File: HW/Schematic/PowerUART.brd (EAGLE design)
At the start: 29.1 x 35.4 mm, 62 parts, among them U2 CP2104

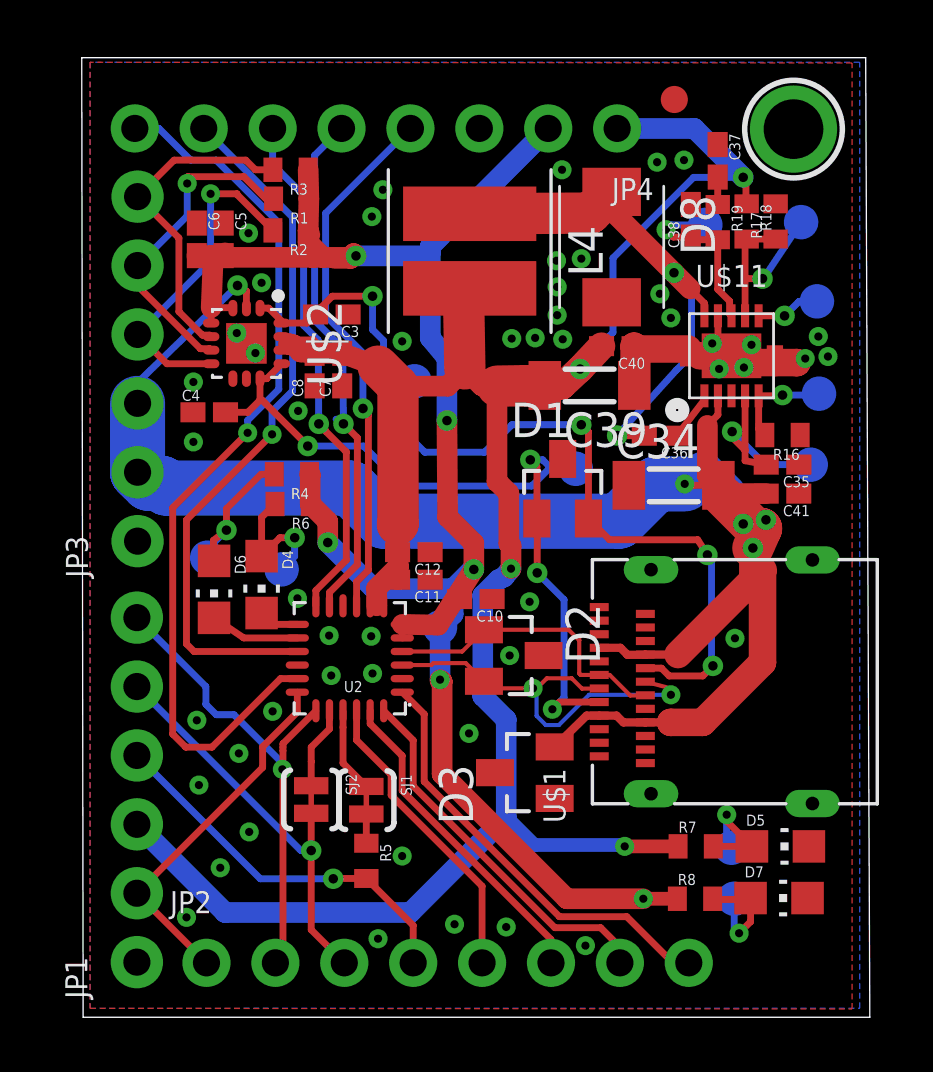
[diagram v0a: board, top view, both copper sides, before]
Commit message: Add labels
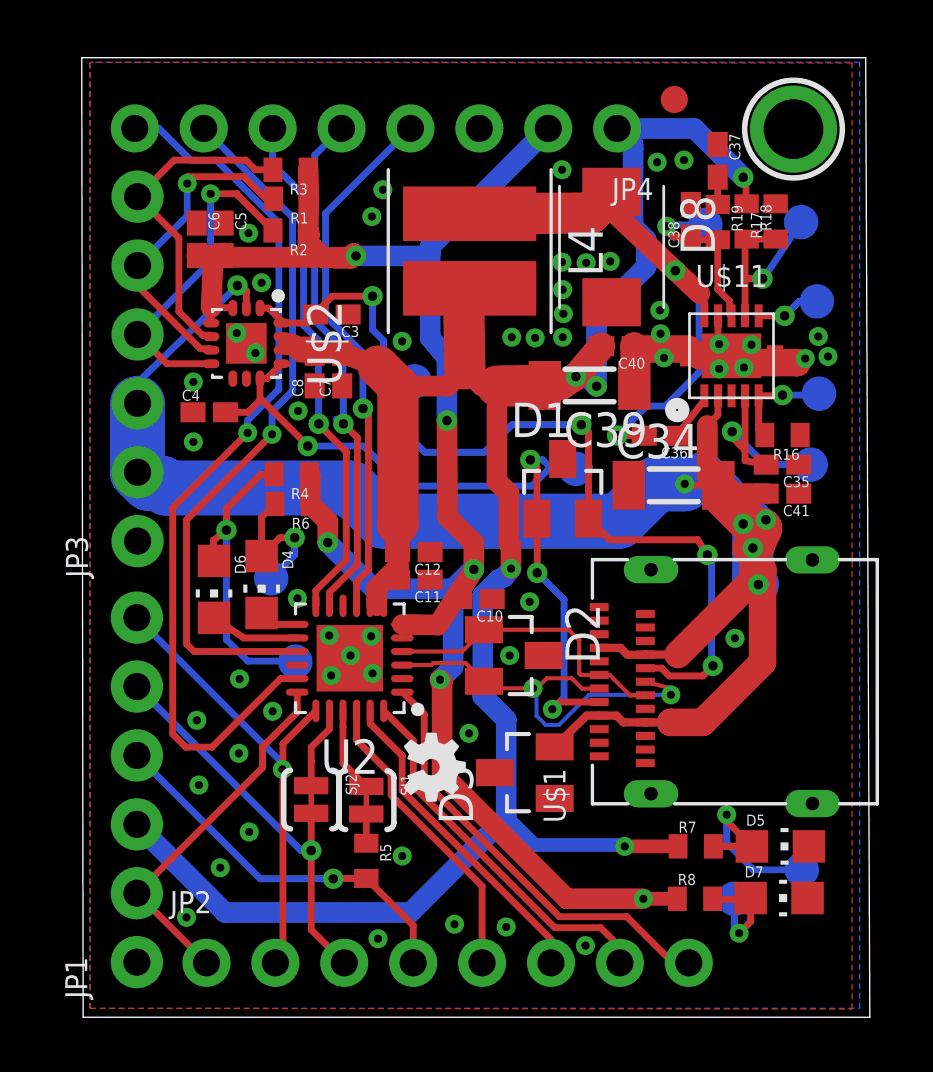
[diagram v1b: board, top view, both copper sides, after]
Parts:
- removed TP10, TP16, TP5, TP6: CP_RESET, testpad:B1,27
- added 5VLEDWP, RXLEDWP, TXLEDWP: CP_RESET, testpad:B1,27
- added LOGO1: OSHW-LOGOMINI, IO_expander:OSHW-LOGO-MINI
- U2: value CP2104 -> CP2104QFN_PAD; device CP2104:QFN50P400X400X100-24 -> CP2104:QFN50P400X400X80-25T245
- renumbered TP1 to SS/TR, TP11 to PGOOD, TP12 to 3V45LEDWP, TP3 to CLK, TP4 to VSNS, TP7 to CC1, TP8 to CC2, TP9 to COMP
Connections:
- net 5VLEDWP: now also 5VLEDWP.TP; no longer TP10.TP
- net CP_VDD_3V45: no longer TP16.TP
- net GND: now also U2.25
- net RXLEDWP: now also RXLEDWP.TP; no longer TP6.TP
- net TXLEDWP: now also TXLEDWP.TP; no longer TP5.TP
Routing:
- net TXLEDWP: track 5.75 -> 11.4 mm
- net 5V: track 90.5 -> 93.6 mm, vias 4 -> 5
- net 5VLEDWP: track 4.27 -> 7.20 mm
- net VBUS: track 68.0 -> 70.5 mm, vias 5 -> 6
- net L1: track 19.9 -> 20.7 mm
- net GND: track 8.31 -> 8.25 mm, vias 50 -> 54
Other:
- board text added: "/INT"
- board text added: "/SUS"
- board text added: "20V 5A max"
- board text added: "3v45"
- board text added: "5V"
- board text added: "CTS"
- board text added: "DCD"
- board text added: "DSR"
- board text added: "DTR"
- board text added: "Engineerd by @bindebende REV A 2018.11.24. github.com/ bindebende/PowerUART"
- board text added: "GND"
- board text added: "GPIO2"
- board text added: "GPIO3"
- board text added: "RESET"
- board text added: "RI"
- board text added: "RTS"
- board text added: "RXD"
- board text added: "SCL"
- board text added: "SDA"
- board text added: "SUS"
- board text added: "TXD"
- board text added: "VBUS"

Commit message: add testpoints.csv
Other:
- board size 29.1 x 35.4 mm -> 29 x 35.5 mm
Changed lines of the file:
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@@
 <setting verticaltext="up"/>
 </settings>
-<grid distance="1" unitdist="mil" unit="mil" style="lines" multiple="1" display="yes" altdistance="0.000123031496" altunitdist="mil" altunit="mil"/>
+<grid distance="1" unitdist="mil" unit="mm" style="lines" multiple="1" display="yes" altdistance="0.000123031496" altunitdist="mil" altunit="mil"/>
 <layers>
 <layer number="1" name="Top" color="4" fill="1" visible="yes" active="yes"/>
@@
 <fusionsync huburn="a.cGVyc29uYWw6dWUyOTdhZGZi" projecturn="a.cGVyc29uYWw6dWUyOTdhZGZiIzIwMTYwMTA4MjIzOTY3MjY" f3durn="urn:adsk.wipprod:dm.lineage:jQXCEEFlSgyEhEQMhi0FtQ" pcbguid="53d00ac5-8cbc-41ab-bffd-7753b437712b" lastpulledtime="" lastsyncedchangeguid="e1987d31-fde6-4ada-60cd-040e15f8273c"/>
 <plain>
-<wire x1="0" y1="0" x2="29" y2="0" width="0" layer="20"/>
-<wire x1="29" y1="0" x2="28.8476" y2="35.3736" width="0" layer="20"/>
-<wire x1="28.8476" y1="35.3736" x2="-0.0508" y2="35.3736" width="0" layer="20"/>
-<wire x1="-0.0508" y1="35.3736" x2="0" y2="0" width="0" layer="20"/>
+<wire x1="0" y1="0" x2="1.1938" y2="0" width="0" layer="20"/>
+<wire x1="1.1938" y1="0" x2="29" y2="0" width="0" layer="20"/>
+<wire x1="29" y1="0" x2="29" y2="35.5" width="0" layer="20"/>
+<wire x1="29" y1="35.5" x2="0" y2="35.5" width="0" layer="20"/>
+<wire x1="0" y1="35.5" x2="0" y2="34.1376" width="0" layer="20"/>
 <text x="25.1968" y="27.3558" size="1.27" layer="38" font="vector" rot="MR270">Engineerd by
 @bindebende
@@
 <text x="3.2258" y="29.7434" size="1.016" layer="26" font="vector" rot="MR180">/INT</text>
 <text x="3.113153125" y="32.11484375" size="1.016" layer="26" font="vector" rot="MR225">SUS</text>
+<wire x1="0" y1="34.1376" x2="0" y2="1.1938" width="0" layer="20"/>
+<wire x1="0" y1="1.1938" x2="0" y2="0" width="0" layer="20"/>
 <wire x1="5.7912" y1="31.5214" x2="5.8166" y2="31.496" width="0.254" layer="26"/>
 <text x="3.2004" y="34.9504" size="1.016" layer="26" font="vector" rot="MR180">/SUS</text>
@@
 <wire x1="6.985" y1="23.7744" x2="4.572" y2="23.7744" width="0.254" layer="26"/>
 <text x="8.9154" y="18.8976" size="1.016" layer="26" font="vector" rot="MR90">20V 5A max</text>
+<wire x1="1.362696875" y1="35.500296875" x2="1.365834375" y2="35.500296875" width="0.000003125" layer="20"/>
 </plain>
 <attributes>

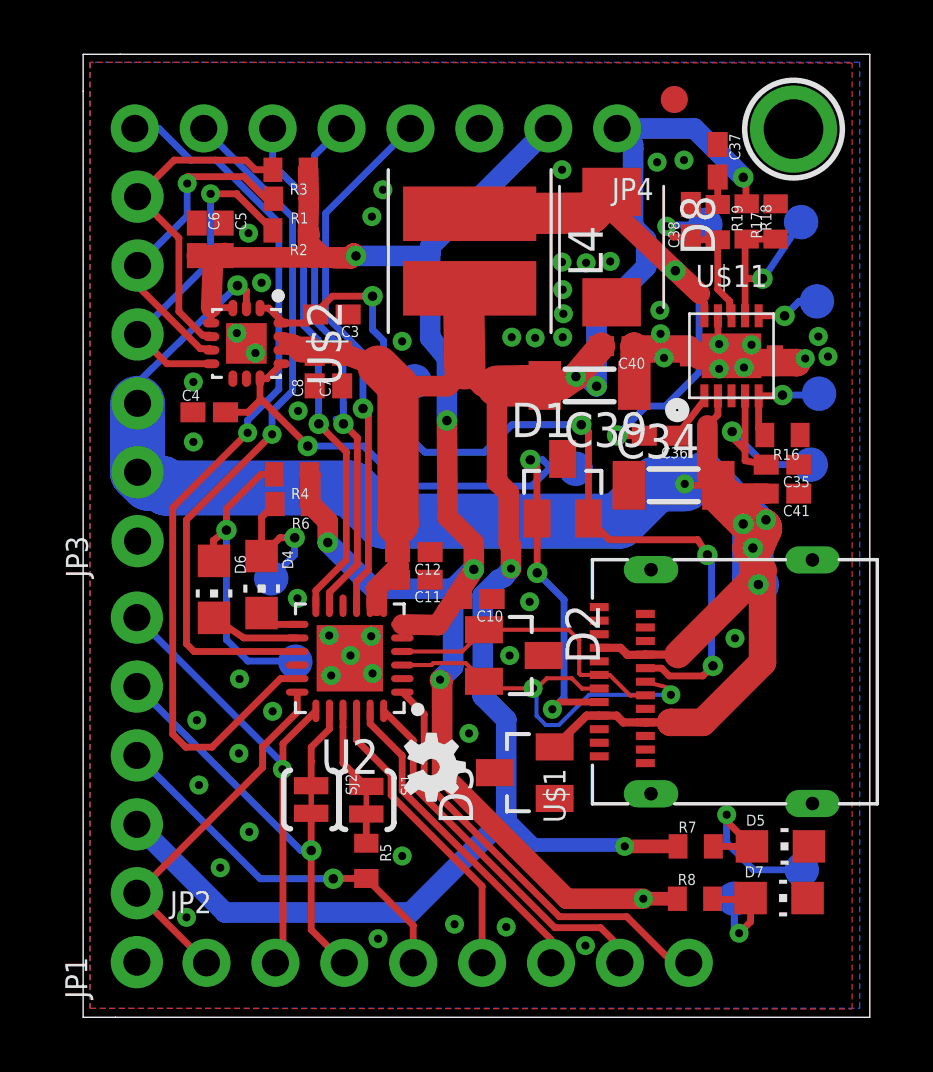
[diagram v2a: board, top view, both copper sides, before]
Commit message: Add silta based EOL Tests
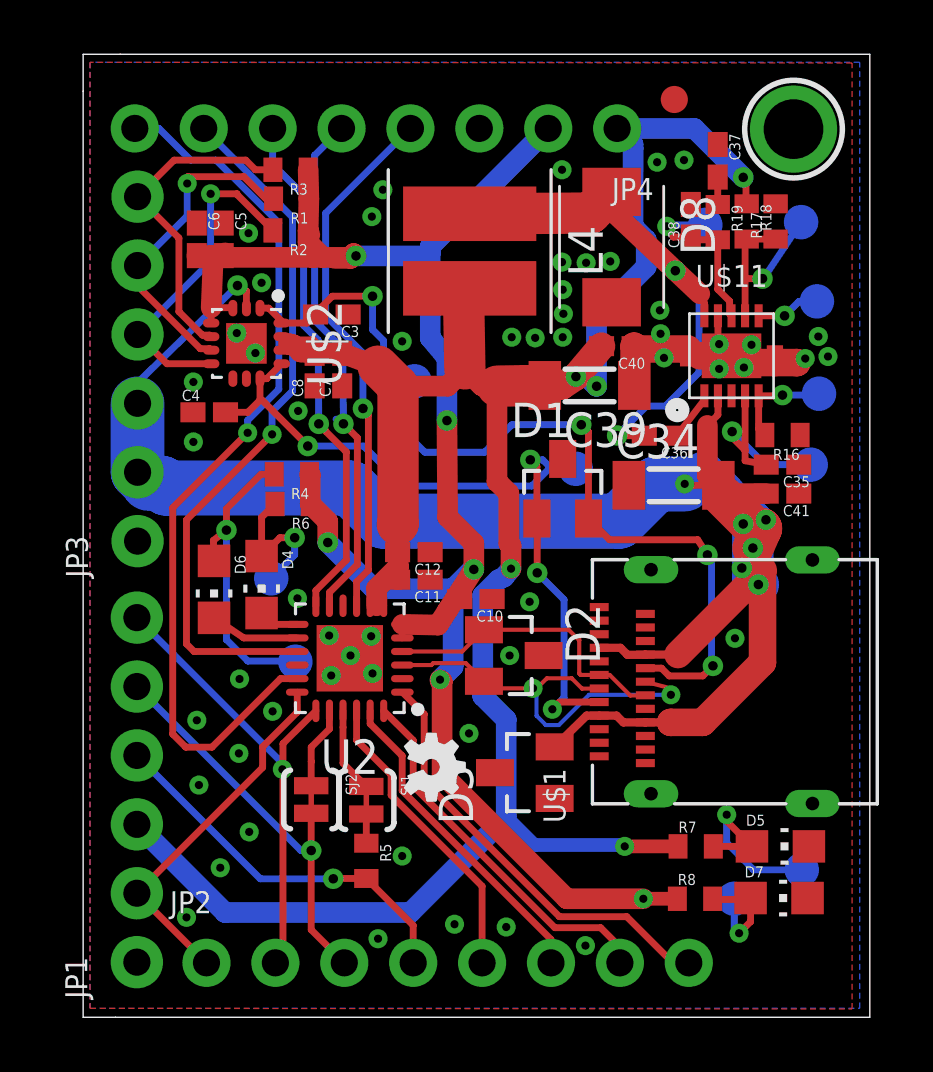
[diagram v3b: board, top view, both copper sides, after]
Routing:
- net VBUS: track 70.5 -> 70.2 mm, vias 6 -> 7
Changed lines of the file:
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@@
 <setting verticaltext="up"/>
 </settings>
-<grid distance="1" unitdist="mil" unit="mm" style="lines" multiple="1" display="yes" altdistance="0.000123031496" altunitdist="mil" altunit="mil"/>
+<grid distance="1" unitdist="mil" unit="mil" style="lines" multiple="1" display="yes" altdistance="0.000123031496" altunitdist="mil" altunit="mil"/>
 <layers>
 <layer number="1" name="Top" color="4" fill="1" visible="yes" active="yes"/>
@@
 <wire x1="21.124625" y1="19.661890625" x2="19.750734375" y2="18.288" width="2.032" layer="16"/>
 <wire x1="22.176490625" y1="19.661890625" x2="21.124625" y2="19.661890625" width="2.032" layer="16"/>
-<wire x1="2.0066" y1="22.6314" x2="2.0066" y2="20.0914" width="2.032" layer="16"/>
+<wire x1="2.0066" y1="22.6314" x2="2.0066" y2="20.0914" width="1.9812" layer="16"/>
 <via x="5.6896" y="26.9748" extent="1-16" drill="0.35"/>
 <wire x1="5.6896" y1="26.9748" x2="2.0066" y2="23.3934" width="0.254" layer="16"/>
 <wire x1="2.0066" y1="23.3934" x2="2.0066" y2="22.6314" width="0.254" layer="16"/>
-<wire x1="2.0066" y1="20.0914" x2="2.2098" y2="19.8882" width="2.032" layer="16"/>
 <wire x1="9.8552" y1="19.5072" x2="11.0744" y2="18.288" width="2.032" layer="16"/>
 <wire x1="2.89036875" y1="19.685" x2="3.06816875" y2="19.5072" width="2.032" layer="16"/>
 <wire x1="2.413" y1="19.685" x2="2.89036875" y2="19.685" width="2.032" layer="16"/>
-<wire x1="2.0066" y1="20.0914" x2="2.413" y2="19.685" width="2.032" layer="16"/>
+<wire x1="2.0066" y1="20.0914" x2="2.413" y2="19.685" width="1.9812" layer="16"/>
 <wire x1="3.06816875" y1="19.5072" x2="9.8552" y2="19.5072" width="2.032" layer="16"/>
 <wire x1="6.0198" y1="26.1412" x2="6.0198" y2="26.7716" width="0.254" layer="1"/>
@@
 <wire x1="24.6888" y1="17.2974" x2="24.6888" y2="16.1544" width="1.524" layer="16"/>
 <wire x1="24.6888" y1="16.1544" x2="24.892" y2="15.9512" width="1.524" layer="16"/>
+<via x="24.2824" y="16.5608" extent="1-16" drill="0.35"/>
+<wire x1="24.6888" y1="16.1544" x2="24.2824" y2="16.5608" width="0" layer="19" extent="16-16"/>
 </signal>
 <signal name="CP_RESET">
